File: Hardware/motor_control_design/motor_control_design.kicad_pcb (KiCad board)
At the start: 2 copper layers, 57.1 x 57.2 mm, 0 parts

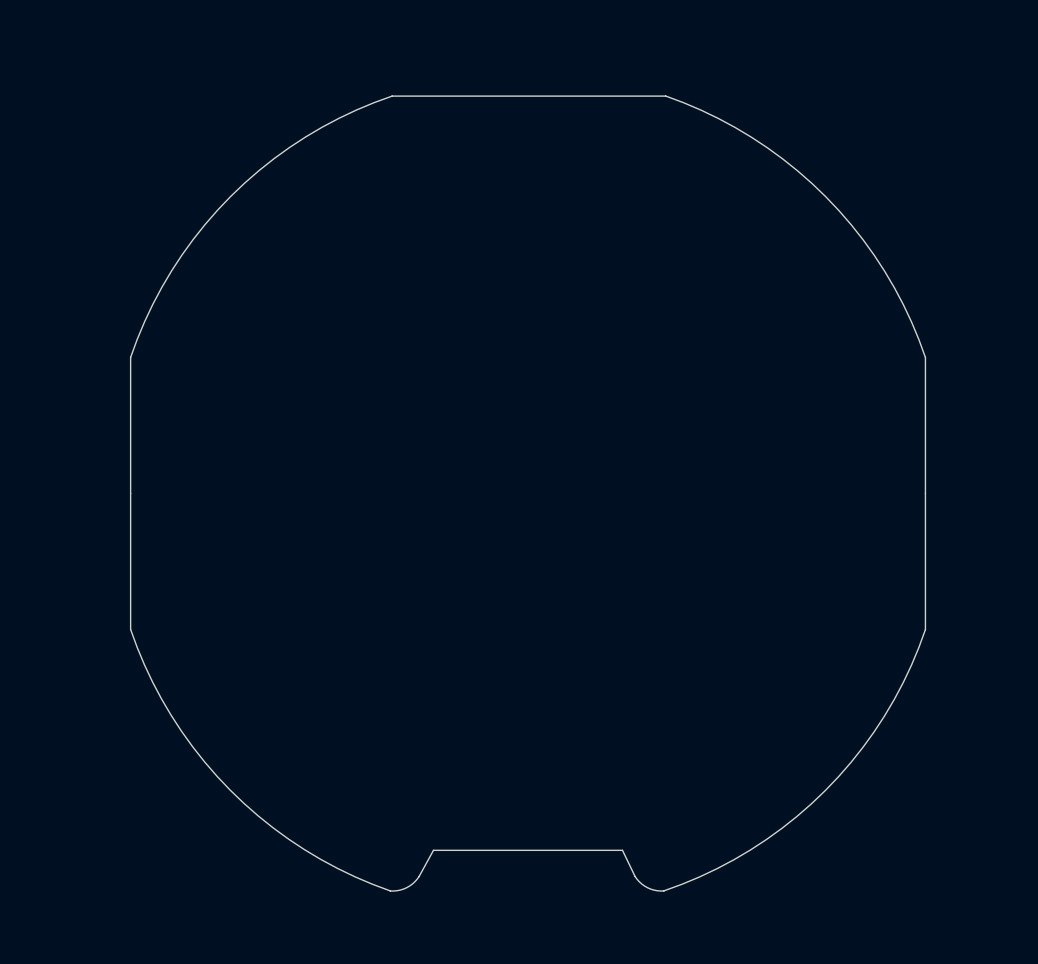
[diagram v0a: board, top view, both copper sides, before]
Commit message: Finished motor controller schematic and routing
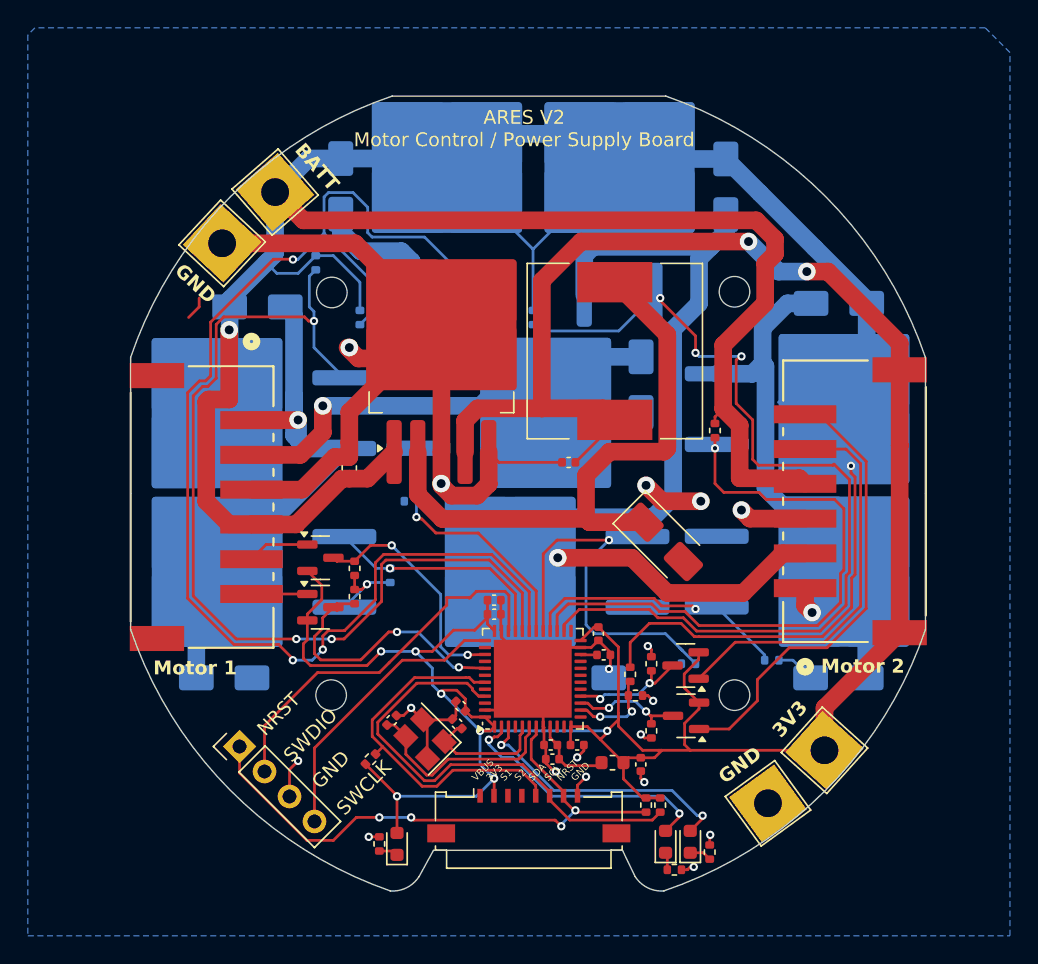
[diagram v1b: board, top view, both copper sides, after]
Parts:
- added ?: , , F.Cu at (134.9, 74.7)
- added ?: , , F.Cu at (134.8, 103.6)
- added ?: , , F.Cu at (163.8, 74.6)
- added ?: , , F.Cu at (163.8, 103.6)
- added C1: 10uF, Capacitor_SMD:C_0402_1005Metric, F.Cu at (146.6, 96.8)
- added C10: 1uF, Capacitor_SMD:C_0402_1005Metric, F.Cu at (150.7, 108.2)
- added C11: 1uF, Capacitor_SMD:C_0402_1005Metric, F.Cu at (157.1, 108.6)
- added C14: 100uF, Capacitor_SMD:C_0603_1608Metric, F.Cu at (136.1, 87.3)
- added C15: 330uF, Capacitor_SMD:C_0402_1005Metric, F.Cu at (151.9, 86.9)
- added C2: 10pF, Capacitor_SMD:C_0402_1005Metric, F.Cu at (143.9, 105.7)
- added C3: 100nF, Capacitor_SMD:C_0402_1005Metric, F.Cu at (152.5, 107.2)
- added C4: 100nF, Capacitor_SMD:C_0402_1005Metric, F.Cu at (144.1, 104.4)
- added C5: 10pF, Capacitor_SMD:C_0402_1005Metric, F.Cu at (139.2, 105.4)
- added C6: 100nF, Capacitor_SMD:C_0402_1005Metric, F.Cu at (154.1, 99.2)
- added C7: 2.2uF, Capacitor_SMD:C_0402_1005Metric, F.Cu at (154.4, 100.7)
- added C8: 100nF, Capacitor_SMD:C_0402_1005Metric, F.Cu at (146.6, 97.8)
- added C9: 10nF, Capacitor_SMD:C_0402_1005Metric, F.Cu at (150.6, 107.2)
- added D1: LED, LED_SMD:LED_0603_1608Metric, F.Cu at (139.6, 114.3)
- added D10: SS34, Diode_SMD:D_SMA, B.Cu at (163.2, 67.1)
- added D11: SS34, Diode_SMD:D_SMA, F.Cu at (158.8, 92.6)
- added D12: SS34, Diode_SMD:D_SMA, B.Cu at (152.8, 102.4)
- added D2: LED, LED_SMD:LED_0603_1608Metric, F.Cu at (158.9, 114.1)
- added D3: LED, LED_SMD:LED_0603_1608Metric, F.Cu at (160.7, 114.1)
- added D4: SS34, Diode_SMD:D_SMA, B.Cu at (129.5, 75.7)
- added D5: SS34, Diode_SMD:D_SMA, B.Cu at (127.1, 102.4)
- added D6: SS34, Diode_SMD:D_SMA, B.Cu at (157.1, 81.3)
- added D7: SS34, Diode_SMD:D_SMA, B.Cu at (135.5, 67.0)
- added D8: SS34, Diode_SMD:D_SMA, B.Cu at (171.3, 75.4)
- added D9: SS34, Diode_SMD:D_SMA, B.Cu at (171.3, 102.4)
- added FB1: 120R, Inductor_SMD:L_0603_1608Metric, F.Cu at (155.1, 108.5)
- added G***: LOGO, LOGO, B.Cu at (149.2, 107.3)
- added J10: 3V3, TestPoint:TestPoint_THTPad_4.0x4.0mm_Drill2.0mm, F.Cu at (170.3, 107.6)
- added J2: SWD, Connector_PinHeader_2.54mm:PinHeader_1x04_P2.54mm_Vertical, F.Cu at (128.3, 107.3)
- added J3: VBAT, TestPoint:TestPoint_THTPad_4.0x4.0mm_Drill2.0mm, F.Cu at (130.8, 67.4)
- added J4: GND, TestPoint:TestPoint_THTPad_4.0x4.0mm_Drill2.0mm, F.Cu at (127.0, 71.1)
- added J5: FC_M/P, Connector_FFC-FPC:Molex_200528-0080_1x08-1MP_P1.00mm_Horizontal, F.Cu at (149.0, 111.7)
- added J6: Conn_01x06, JST-XH-SMD:CONN_S6B-XH-SM4-TB_JST, F.Cu at (125.6, 90.1)
- added J8: Conn_01x06, JST-XH-SMD:CONN_S6B-XH-SM4-TB_JST, F.Cu at (172.5, 89.7)
- added J9: GND, TestPoint:TestPoint_THTPad_4.0x4.0mm_Drill2.0mm, F.Cu at (166.2, 111.4)
- added L1: 100uH, Inductor_SMD:L_12x12mm_H4.5mm, F.Cu at (155.2, 78.9)
- added Q1: RF1S9540SM, Package_TO_SOT_SMD:TO-263-2, B.Cu at (143.2, 67.2)
- added Q10: 2N7002, Package_TO_SOT_SMD:SOT-23, F.Cu at (134.1, 97.3)
- added Q11: 2N7002, Package_TO_SOT_SMD:SOT-23, F.Cu at (160.4, 105.1)
- added Q12: 2N7002, Package_TO_SOT_SMD:SOT-23, F.Cu at (160.3, 101.5)
- added Q2: RF1S9540SM, Package_TO_SOT_SMD:TO-263-2, B.Cu at (128.1, 83.3)
- added Q3: IRLZ44NS, Package_TO_SOT_SMD:TO-263-2, B.Cu at (148.8, 83.3)
- added Q4: RF1S9540SM, Package_TO_SOT_SMD:TO-263-2, B.Cu at (170.2, 83.0)
- added Q5: IRLZ44NS, Package_TO_SOT_SMD:TO-263-2, B.Cu at (170.2, 94.7)
- added Q6: RF1S9540SM, Package_TO_SOT_SMD:TO-263-2, B.Cu at (155.6, 67.2)
- added Q7: IRLZ44NS, Package_TO_SOT_SMD:TO-263-2, B.Cu at (149.2, 94.7)
- added Q8: 2N7002, Package_TO_SOT_SMD:SOT-23, F.Cu at (134.1, 93.7)
- added Q9: IRLZ44NS, Package_TO_SOT_SMD:TO-263-2, B.Cu at (128.1, 94.7)
- added R1: 4.7k, Resistor_SMD:R_0402_1005Metric, F.Cu at (137.7, 108.2)
- added R10: 1k, Resistor_SMD:R_0402_1005Metric, F.Cu at (136.5, 96.5)
- added R11: 29.4k, Resistor_SMD:R_0402_1005Metric, F.Cu at (156.3, 102.1)
- added R12: 10k, Resistor_SMD:R_0402_1005Metric, F.Cu at (156.7, 103.6)
- added R13: 10k, Resistor_SMD:R_0402_1005Metric, B.Cu at (133.7, 72.5)
- added R14: 10k, Resistor_SMD:R_0402_1005Metric, B.Cu at (136.9, 76.5)
- added R15: 10k, Resistor_SMD:R_0402_1005Metric, B.Cu at (140.6, 89.7)
- added R16: 10k, Resistor_SMD:R_0402_1005Metric, B.Cu at (139.1, 95.0)
- added R17: 10k, Resistor_SMD:R_0402_1005Metric, F.Cu at (162.4, 84.6)
- added R18: 10k, Resistor_SMD:R_0402_1005Metric, B.Cu at (166.5, 101.1)
- added R19: 10k, Resistor_SMD:R_0402_1005Metric, B.Cu at (149.4, 76.5)
- added R2: 4.7k, Resistor_SMD:R_0402_1005Metric, F.Cu at (158.5, 111.5)
- added R20: 10k, Resistor_SMD:R_0402_1005Metric, B.Cu at (160.5, 101.3)
- added R21: 1k, Resistor_SMD:R_0402_1005Metric, F.Cu at (157.9, 106.2)
- added R22: 1k, Resistor_SMD:R_0402_1005Metric, F.Cu at (157.9, 101.3)
- added R3: 10k, Resistor_SMD:R_0402_1005Metric, F.Cu at (157.5, 111.5)
- added R5: 1k, Resistor_SMD:R_0402_1005Metric, F.Cu at (138.3, 114.3)
- added R7: 1k, Resistor_SMD:R_0402_1005Metric, F.Cu at (159.5, 116.2)
- added R8: 1k, Resistor_SMD:R_0402_1005Metric, F.Cu at (162.1, 114.9)
- added R9: 1k, Resistor_SMD:R_0402_1005Metric, F.Cu at (136.5, 94.5)
- added U1: STM32F401CCU6, Package_DFN_QFN:QFN-48-1EP_7x7mm_P0.5mm_EP5.6x5.6mm, F.Cu at (149.3, 102.4)
- added U3: LM2576S-3.3, Package_TO_SOT_SMD:TO-263-5_TabPin3, F.Cu at (142.8, 78.5)
- added Y1: 16MHz, Crystal:Crystal_SMD_3225-4Pin_3.2x2.5mm, F.Cu at (141.6, 106.8)
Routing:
- net +BATT: track 0.00 -> 212.2 mm, vias 0 -> 2
- net +3.3V: track 0.00 -> 204.9 mm, vias 0 -> 9
- net GND: track 0.00 -> 125.0 mm, vias 0 -> 19
- net /M1Q3: track 0.00 -> 94.0 mm, vias 0 -> 3
- net /M2B: track 0.00 -> 69.6 mm, vias 0 -> 1
- net /M1Q1: track 0.00 -> 69.4 mm, vias 0 -> 3
- net /M2Q3: track 0.00 -> 66.0 mm, vias 0 -> 3
- net /M1B: track 0.00 -> 49.3 mm, vias 0 -> 1
- net Net-(D11-K): track 0.00 -> 43.4 mm
- net /M2Q1: track 0.00 -> 43.3 mm, vias 0 -> 1
- net /NRST: track 0.00 -> 42.3 mm, vias 0 -> 4
- net /M1A: track 0.00 -> 35.7 mm, vias 0 -> 1
- net /SCL: track 0.00 -> 34.6 mm
- net Net-(J8-Pin_6): track 0.00 -> 32.9 mm
- net /M2A: track 0.00 -> 31.1 mm, vias 0 -> 1
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- added copper zone on B.Cu, net GND
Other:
- board text added: "3V3"
- board text added: "ARES V2 Motor Control / Power Supply Board"
- board text added: "BATT"
- board text added: "CIRCLE CENTER"
- board text added: "CIRCLE EDGE"
- board text added: "GND"
- board text added: "Motor 1"
- board text added: "Motor 2"
- board text added: "NRST"
- board text added: "S1"
- board text added: "S2"
- board text added: "SCL"
- board text added: "SDA"
- board text added: "SWCLK"
- board text added: "SWDIO"
- board text added: "VBUS"
